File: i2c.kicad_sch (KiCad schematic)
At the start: 22 parts, among them U16 PCA9517A_TSSOP, U23 TS5A3359_VSSOP, U24 TS5A3359_VSSOP

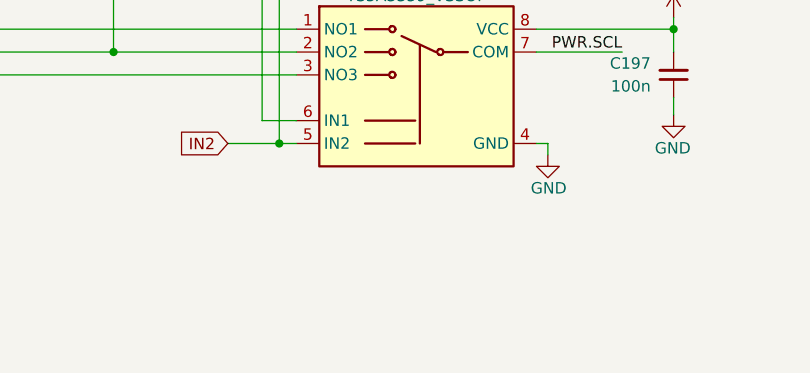
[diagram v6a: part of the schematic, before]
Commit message: 55007 README: Add photo
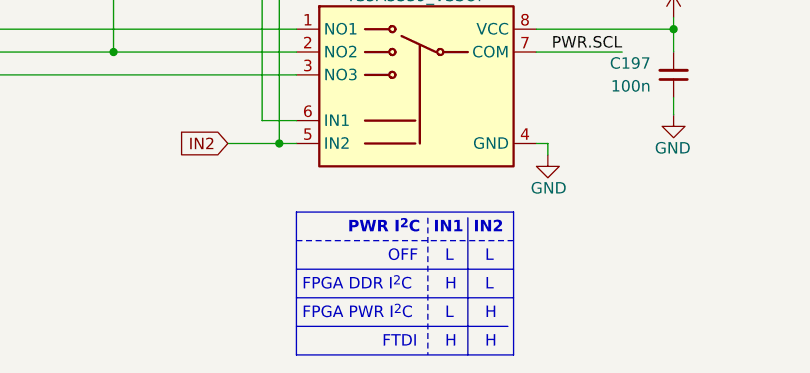
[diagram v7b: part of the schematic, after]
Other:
- note added: "FPGA DDR I^{2}C"
- note added: "FPGA PWR I^{2}C"
- note added: "FTDI"
- note added: "H"
- note added: "IN1"
- note added: "IN2"
- note added: "L"
- note added: "OFF"
- note added: "PWR I^{2}C"
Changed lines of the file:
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@@
     (stroke (width 0) (type default) (color 0 0 0 0))
+  )
+  (polyline (pts (xy 143.51 234.315) (xy 167.64 234.315))
+    (stroke (width 0) (type dash) (color 0 0 0 0))
   )
   (wire (pts (xy 94.615 210.82) (xy 143.51 210.82))
@@
     (stroke (width 0) (type default) (color 0 0 0 0))
   )
+  (polyline (pts (xy 143.51 231.14) (xy 167.64 231.14))
+    (stroke (width 0) (type default) (color 0 0 0 0))
+  )
   (wire (pts (xy 250.19 207.645) (xy 287.02 207.645))
     (stroke (width 0) (type default) (color 0 0 0 0))
@@
     (stroke (width 0) (type default) (color 0 0 0 0))
   )
+  (polyline (pts (xy 167.64 247.015) (xy 143.51 247.015))
+    (stroke (width 0) (type default) (color 0 0 0 0))
+  )
   (wire (pts (xy 238.125 201.295) (xy 287.02 201.295))
     (stroke (width 0) (type default) (color 0 0 0 0))
@@
     (stroke (width 0) (type default) (color 0 0 0 0))
   )
+  (polyline (pts (xy 162.56 231.775) (xy 162.56 247.015))
+    (stroke (width 0) (type default) (color 0 0 0 0))
+  )
   (wire (pts (xy 300.99 207.645) (xy 311.785 207.645))
     (stroke (width 0) (type default) (color 0 0 0 0))
@@
     (stroke (width 0) (type default) (color 0 0 0 0))
   )
+  (polyline (pts (xy 143.51 231.14) (xy 143.51 247.015))
+    (stroke (width 0) (type default) (color 0 0 0 0))
+  )
   (wire (pts (xy 300.99 201.295) (xy 292.1 201.295))
     (stroke (width 0) (type default) (color 0 0 0 0))
@@
     (stroke (width 0) (type default) (color 0 0 0 0))
   )
+  (polyline (pts (xy 167.64 231.14) (xy 167.64 247.015))
+    (stroke (width 0) (type default) (color 0 0 0 0))
+  )
   (bus (pts (xy 166.37 81.28) (xy 166.37 82.55))
     (stroke (width 0) (type default) (color 0 0 0 0))
@@
     (stroke (width 0) (type default) (color 0 0 0 0))
   )
+  (polyline (pts (xy 143.51 240.665) (xy 167.64 240.665))
+    (stroke (width 0) (type default) (color 0 0 0 0))
+  )
   (wire (pts (xy 238.125 210.185) (xy 287.02 210.185))
     (stroke (width 0) (type default) (color 0 0 0 0))
@@
     (stroke (width 0) (type default) (color 0 0 0 0))
   )
+  (polyline (pts (xy 158.115 231.775) (xy 158.115 247.015))
+    (stroke (width 0) (type dash) (color 0 0 0 0))
+  )
   (bus (pts (xy 271.145 80.645) (xy 270.51 81.28))
     (stroke (width 0) (type default) (color 0 0 0 0))
@@
     (stroke (width 0) (type default) (color 0 0 0 0))
   )
+  (polyline (pts (xy 143.51 237.49) (xy 167.64 237.49))
+    (stroke (width 0) (type default) (color 0 0 0 0))
+  )
   (wire (pts (xy 235.585 84.455) (xy 235.585 85.09))
     (stroke (width 0) (type default) (color 0 0 0 0))
   )
+  (polyline (pts (xy 143.51 243.84) (xy 167.005 243.84))
+    (stroke (width 0) (type default) (color 0 0 0 0))
+  )
   (wire (pts (xy 253.365 67.945) (xy 253.365 65.405))
     (stroke (width 0) (type default) (color 0 0 0 0))
@@
   (wire (pts (xy 143.51 196.85) (xy 139.7 196.85))
     (stroke (width 0) (type default) (color 0 0 0 0))
+  )
+  (text "L" (at 164.465 240.03 0)
+    (effects (font (size 1.27 1.27)) (justify left bottom))
   )
   (text "PWR I2C MUX" (at 15.24 142.24 0)
     (effects (font (size 2.54 2.54) (thickness 0.4978) bold) (justify left bottom))
   )
+  (text "L" (at 160.02 243.205 0)
+    (effects (font (size 1.27 1.27)) (justify left bottom))
+  )
+  (text "FTDI" (at 153.035 246.38 0)
+    (effects (font (size 1.27 1.27)) (justify left bottom))
+  )
+  (text "H" (at 164.465 243.205 0)
+    (effects (font (size 1.27 1.27)) (justify left bottom))
+  )
+  (text "H" (at 160.02 246.38 0)
+    (effects (font (size 1.27 1.27)) (justify left bottom))
+  )
+  (text "OFF" (at 153.67 236.855 0)
+    (effects (font (size 1.27 1.27)) (justify left bottom))
+  )
+  (text "PWR I^{2}C" (at 149.225 233.68 0)
+    (effects (font (size 1.27 1.27) (thickness 0.254) bold) (justify left bottom))
+  )
   (text "I2C logic translator" (at 15.875 19.685 0)
     (effects (font (size 2.54 2.54) (thickness 0.4978) bold) (justify left bottom))
   )
+  (text "H" (at 164.465 246.38 0)
+    (effects (font (size 1.27 1.27)) (justify left bottom))
+  )
   (text "0R Mux bypass" (at 283.845 187.325 0)
     (effects (font (size 1.27 1.27)) (justify left bottom))
   )
+  (text "H" (at 160.02 240.03 0)
+    (effects (font (size 1.27 1.27)) (justify left bottom))
+  )
+  (text "IN2" (at 163.195 233.68 0)
+    (effects (font (size 1.27 1.27) (thickness 0.254) bold) (justify left bottom))
+  )
+  (text "L" (at 160.02 236.855 0)
+    (effects (font (size 1.27 1.27)) (justify left bottom))
+  )
+  (text "IN1" (at 158.75 233.68 0)
+    (effects (font (size 1.27 1.27) (thickness 0.254) bold) (justify left bottom))
+  )
+  (text "L" (at 164.465 236.855 0)
+    (effects (font (size 1.27 1.27)) (justify left bottom))
+  )
+  (text "FPGA PWR I^{2}C" (at 144.145 243.205 0)
+    (effects (font (size 1.27 1.27)) (justify left bottom))
+  )
+  (text "FPGA DDR I^{2}C" (at 144.145 240.03 0)
+    (effects (font (size 1.27 1.27)) (justify left bottom))
+  )

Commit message: [#57478] ohp release
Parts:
- C165, C166, C196, C197: footprint sodimm-ddr5-tester-footprints:C_0402_1005Metric -> antmicro-footprints:C_0402_1005Metric; symbol sodimm-ddr5-tester:C_100n_0402 -> antmicroCapacitors0402:C_100n_0402
- R122, R123, R124, R125, R150, R159: footprint sodimm-ddr5-tester-footprints:R_0402_1005Metric -> antmicro-footprints:R_0402_1005Metric; symbol sodimm-ddr5-tester:R_4k7_0402 -> antmicroResistors0402:R_4k7_0402
- R126, R174, R175, R176, R177, R178, R179: footprint sodimm-ddr5-tester-footprints:R_0402_1005Metric -> antmicro-footprints:R_0402_1005Metric; symbol sodimm-ddr5-tester:R_0R_0402 -> antmicroResistors0402:R_0R_0402; now not fitted; now left out of the parts list
- R127: footprint sodimm-ddr5-tester-footprints:R_0402_1005Metric -> antmicro-footprints:R_0402_1005Metric; symbol sodimm-ddr5-tester:R_0R_0402 -> antmicroResistors0402:R_0R_0402
- TP7: footprint sodimm-ddr5-tester-footprints:TP_SMD_1mm -> antmicro-footprints:TP_SMD_1mm; symbol sodimm-ddr5-tester:TP_1mm_SMD -> antmicroTestPoints:TP_1mm_SMD
- U16: footprint sodimm-ddr5-tester-footprints:TSSOP-8_3x3mm_P0.65mm -> antmicro-footprints:TSSOP-8_3x3mm_P0.65mm; symbol sodimm-ddr5-tester:PCA9517A_TSSOP -> antmicroLogicTranslatorsLevelShifters:PCA9517A_TSSOP
- U23, U24: footprint sodimm-ddr5-tester-footprints:VSSOP-8_2.3x2mm_P0.5mm -> antmicro-footprints:VSSOP-8_2.3x2mm_P0.5mm; symbol sodimm-ddr5-tester:TS5A3359_VSSOP -> antmicroInterfaceAnalogSwitchesMultiplexersDemultiplexers:TS5A3359_VSSOP
